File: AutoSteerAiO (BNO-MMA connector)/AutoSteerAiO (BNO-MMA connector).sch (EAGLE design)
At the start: 83 parts, among them J4 CONNECTOR 1x5 PINS, K4 CB1A-P-12V, U1 VX7805-1000

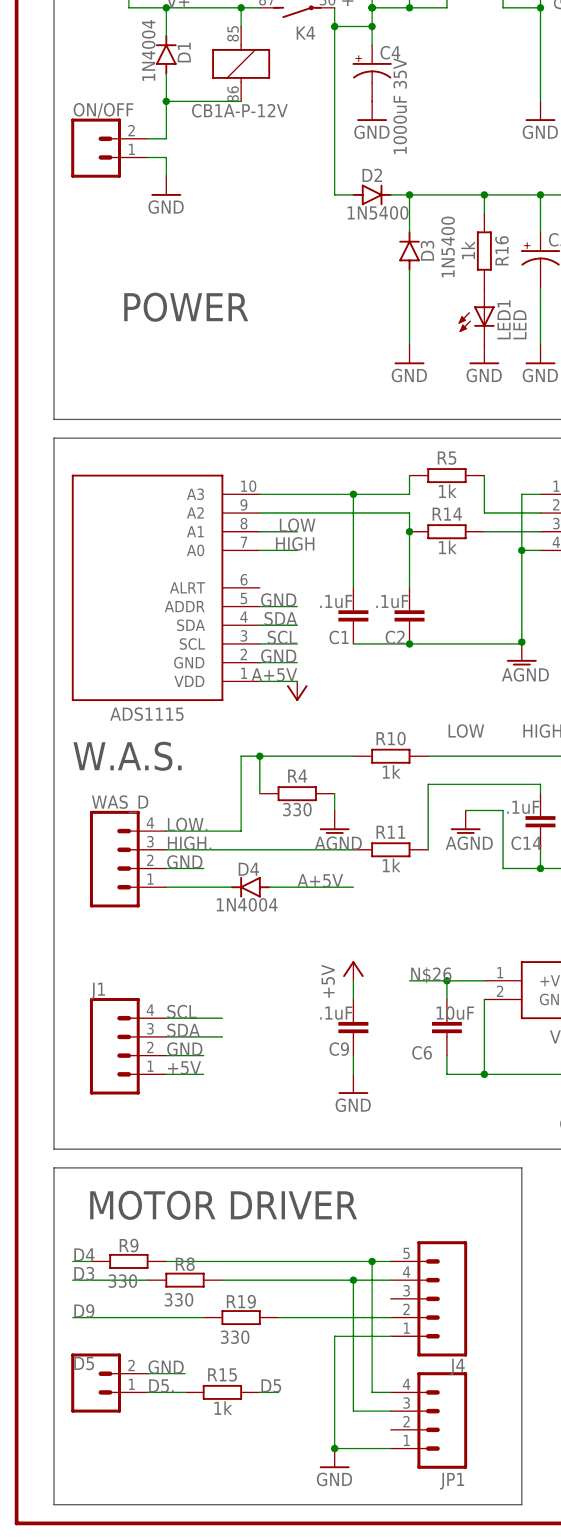
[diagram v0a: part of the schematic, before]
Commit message: Add files via upload
added led autosteer
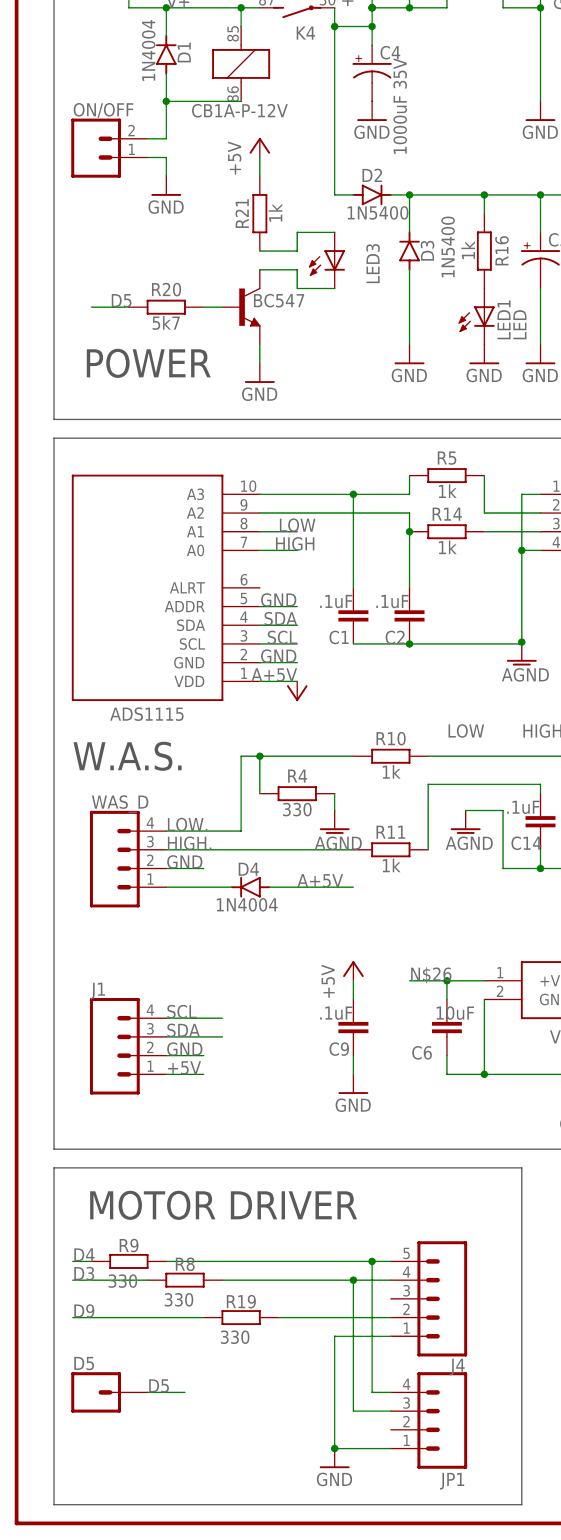
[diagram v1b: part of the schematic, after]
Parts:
- removed R15: 1k, resistor:R-EU_0207/7
- added LED3: LED, adafruit:LED5MM
- added R20: 5k7, resistor:R-EU_0207/7
- added R21: 1k, resistor:R-EU_0207/7
- added T1: BC547, transistor:BC547
- D5: device SparkFun-Connectors:CONN_02 -> SparkFun-Connectors:CONN_01
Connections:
- removed net D5.: D5.1, R15.1
- new net N$23: R20.2, T1.B
- new net N$24: LED3.A, R21.1
- new net N$27: LED3.C, T1.C
- net +5V: now also R21.2
- net D5: now also D5.1, R20.1; no longer R15.2
- net GND: now also T1.E; no longer D5.2
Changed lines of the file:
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@@
 <attribute name="OC_NEWARK" value="unknown"/>
 </part>
-<part name="D5" library="SparkFun-Connectors" library_urn="urn:adsk.eagle:library:513" deviceset="CONN_02" device="" package3d_urn="urn:adsk.eagle:package:38039/1" value="CONNECTOR 1x1 PIN">
+<part name="D5" library="SparkFun-Connectors" library_urn="urn:adsk.eagle:library:513" deviceset="CONN_01" device="" package3d_urn="urn:adsk.eagle:package:38028/1" value="CONNECTOR 1x1 PIN">
 <attribute name="MF" value=""/>
 <attribute name="MPN" value=""/>
@@
 <attribute name="OC_NEWARK" value="unknown"/>
 </part>
-<part name="R15" library="resistor" library_urn="urn:adsk.eagle:library:348" deviceset="R-EU_" device="0207/7" package3d_urn="urn:adsk.eagle:package:23493/2" value="1k">
-<attribute name="MF" value=""/>
-<attribute name="MPN" value=""/>
-<attribute name="OC_NEWARK" value="unknown"/>
-</part>
 <part name="J1" library="SparkFun-Connectors" library_urn="urn:adsk.eagle:library:513" deviceset="CONN_04" device="" package3d_urn="urn:adsk.eagle:package:38085/1"/>
 <part name="J2" library="SparkFun-Connectors" library_urn="urn:adsk.eagle:library:513" deviceset="CONN_05" device="" package3d_urn="urn:adsk.eagle:package:38104/1"/>
@@
 <part name="GND11" library="supply1" library_urn="urn:adsk.eagle:library:371" deviceset="GND" device=""/>
 <part name="P+3" library="supply1" library_urn="urn:adsk.eagle:library:371" deviceset="+5V" device=""/>
+<part name="T1" library="transistor" library_urn="urn:adsk.eagle:library:402" deviceset="BC547" device="" package3d_urn="urn:adsk.eagle:package:28523/2"/>
+<part name="R20" library="resistor" library_urn="urn:adsk.eagle:library:348" deviceset="R-EU_" device="0207/7" package3d_urn="urn:adsk.eagle:package:23493/2" value="5k7">
+<attribute name="MF" value=""/>
+<attribute name="MPN" value=""/>
+<attribute name="OC_NEWARK" value="unknown"/>
+</part>
+<part name="R21" library="resistor" library_urn="urn:adsk.eagle:library:348" deviceset="R-EU_" device="0207/7" package3d_urn="urn:adsk.eagle:package:23493/2" value="1k">
+<attribute name="MF" value=""/>
+<attribute name="MPN" value=""/>
+<attribute name="OC_NEWARK" value="unknown"/>
+</part>
+<part name="P+6" library="supply1" library_urn="urn:adsk.eagle:library:371" deviceset="+5V" device=""/>
+<part name="GND12" library="supply1" library_urn="urn:adsk.eagle:library:371" deviceset="GND" device=""/>
+<part name="LED3" library="adafruit" library_urn="urn:adsk.eagle:library:420" deviceset="LED" device="5MM" package3d_urn="urn:adsk.eagle:package:6240538/1" value="LED">
+<attribute name="MF" value=""/>
+<attribute name="MPN" value=""/>
+<attribute name="OC_NEWARK" value="unknown"/>
+</part>
 </parts>
 <sheets>
@@
 <wire x1="144.78" y1="213.36" x2="144.78" y2="284.48" width="0.1524" layer="97"/>
 <wire x1="144.78" y1="213.36" x2="5.08" y2="213.36" width="0.1524" layer="97"/>
-<text x="22.86" y="228.6" size="3.81" layer="97" font="vector" align="center">POWER</text>
+<text x="17.78" y="220.98" size="3.81" layer="97" font="vector" align="center">POWER</text>
 <wire x1="147.32" y1="198.12" x2="147.32" y2="256.54" width="0.1524" layer="97"/>
 <wire x1="205.74" y1="198.12" x2="147.32" y2="198.12" width="0.1524" layer="97"/>
@@
 <attribute name="MPN" x="152.4" y="276.86" size="1.778" layer="96" display="off"/>
 </instance>
-<instance part="R15" gate="G$1" x="27.94" y="81.28" smashed="yes">
-<attribute name="NAME" x="27.94" y="82.7786" size="1.778" layer="95" rot="R180" align="top-center"/>
-<attribute name="VALUE" x="27.94" y="80.01" size="1.778" layer="95" rot="R180" align="bottom-center"/>
-<attribute name="OC_NEWARK" x="27.94" y="81.28" size="1.778" layer="96" display="off"/>
-<attribute name="MF" x="27.94" y="81.28" size="1.778" layer="96" display="off"/>
-<attribute name="MPN" x="27.94" y="81.28" size="1.778" layer="96" display="off"/>
-</instance>
 <instance part="J1" gate="G$1" x="15.24" y="127" smashed="yes">
 <attribute name="VALUE" x="10.16" y="119.634" size="1.778" layer="96" font="vector"/>
@@
 <instance part="P+3" gate="1" x="111.76" y="190.5" smashed="yes">
 <attribute name="VALUE" x="109.22" y="185.42" size="1.778" layer="96" rot="R90"/>
+</instance>
+<instance part="T1" gate="G$1" x="30.48" y="228.6" smashed="yes">
+<attribute name="VALUE" x="32.004" y="228.6" size="1.778" layer="96"/>
+</instance>
+<instance part="R20" gate="G$1" x="20.32" y="228.6" smashed="yes">
+<attribute name="NAME" x="20.32" y="230.0986" size="1.778" layer="95" rot="R180" align="top-center"/>
+<attribute name="VALUE" x="20.32" y="227.33" size="1.778" layer="95" rot="R180" align="bottom-center"/>
+<attribute name="OC_NEWARK" x="20.32" y="228.6" size="1.778" layer="96" display="off"/>
+<attribute name="MF" x="20.32" y="228.6" size="1.778" layer="96" display="off"/>
+<attribute name="MPN" x="20.32" y="228.6" size="1.778" layer="96" display="off"/>
+</instance>
+<instance part="R21" gate="G$1" x="33.02" y="241.3" smashed="yes" rot="R90">
+<attribute name="NAME" x="31.5214" y="241.3" size="1.778" layer="95" rot="R270" align="top-center"/>
+<attribute name="VALUE" x="34.29" y="241.3" size="1.778" layer="95" rot="R270" align="bottom-center"/>
+<attribute name="OC_NEWARK" x="33.02" y="241.3" size="1.778" layer="96" rot="R90" display="off"/>
+<attribute name="MF" x="33.02" y="241.3" size="1.778" layer="96" rot="R90" display="off"/>
+<attribute name="MPN" x="33.02" y="241.3" size="1.778" layer="96" rot="R90" display="off"/>
+</instance>
+<instance part="P+6" gate="1" x="33.02" y="251.46" smashed="yes">
+<attribute name="VALUE" x="30.48" y="246.38" size="1.778" layer="96" rot="R90"/>
+</instance>
+<instance part="GND12" gate="1" x="33.02" y="218.44" smashed="yes">
+<attribute name="VALUE" x="30.48" y="215.9" size="1.778" layer="96"/>
+</instance>
+<instance part="LED3" gate="G$1" x="43.18" y="236.22" smashed="yes">
+<attribute name="NAME" x="49.276" y="231.648" size="1.778" layer="95" rot="R90"/>
+<attribute name="OC_NEWARK" x="43.18" y="236.22" size="1.778" layer="96" display="off"/>
+<attribute name="MF" x="43.18" y="236.22" size="1.778" layer="96" display="off"/>
+<attribute name="MPN" x="43.18" y="236.22" size="1.778" layer="96" display="off"/>
 </instance>
 </instances>
@@
 <wire x1="96.52" y1="154.94" x2="101.6" y2="154.94" width="0.1524" layer="91"/>
 <label x="96.52" y="154.94" size="1.778" layer="95"/>
+</segment>
+<segment>
+<pinref part="R21" gate="G$1" pin="2"/>
+<pinref part="P+6" gate="1" pin="+5V"/>
+<wire x1="33.02" y1="248.92" x2="33.02" y2="246.38" width="0.1524" layer="91"/>
 </segment>
 </net>
@@
 </segment>
 <segment>
-<pinref part="D5" gate="G$1" pin="2"/>
-<wire x1="17.78" y1="83.82" x2="22.86" y2="83.82" width="0.1524" layer="91"/>
-<label x="17.78" y="83.82" size="1.778" layer="95"/>
-</segment>
-<segment>
 <pinref part="0" gate="J$1" pin="3"/>
 <wire x1="177.8" y1="279.4" x2="180.34" y2="279.4" width="0.1524" layer="91"/>
@@
 <pinref part="GND11" gate="1" pin="GND"/>
 </segment>
+<segment>
+<pinref part="T1" gate="G$1" pin="E"/>
+<pinref part="GND12" gate="1" pin="GND"/>
+<wire x1="33.02" y1="220.98" x2="33.02" y2="223.52" width="0.1524" layer="91"/>
+</segment>
 </net>
 <net name="D5" class="0">
@@
 </segment>
 <segment>
-<pinref part="R15" gate="G$1" pin="2"/>
-<wire x1="33.02" y1="81.28" x2="35.56" y2="81.28" width="0.1524" layer="91"/>
-<label x="33.02" y="81.28" size="1.778" layer="95"/>
+<wire x1="15.24" y1="228.6" x2="10.16" y2="228.6" width="0.1524" layer="91"/>
+<pinref part="R20" gate="G$1" pin="1"/>
+<label x="12.7" y="228.6" size="1.778" layer="95"/>
+</segment>
+<segment>
+<pinref part="D5" gate="G$1" pin="1"/>
+<wire x1="17.78" y1="81.28" x2="22.86" y2="81.28" width="0.1524" layer="91"/>
+<label x="17.78" y="81.28" size="1.778" layer="95"/>
 </segment>
 </net>
@@
 </segment>
 </net>
-<net name="D5." class="0">
-<segment>
-<pinref part="D5" gate="G$1" pin="1"/>
-<wire x1="17.78" y1="81.28" x2="22.86" y2="81.28" width="0.1524" layer="91"/>
-<label x="17.78" y="81.28" size="1.778" layer="95"/>
-<pinref part="R15" gate="G$1" pin="1"/>
-</segment>
-</net>
+<net name="N$23" class="0">
+<segment>
+<wire x1="25.4" y1="228.6" x2="27.94" y2="228.6" width="0.1524" layer="91"/>
+<pinref part="T1" gate="G$1" pin="B"/>
+<pinref part="R20" gate="G$1" pin="2"/>
+</segment>
+</net>
+<net name="N$24" class="0">
+<segment>
+<wire x1="43.18" y1="238.76" x2="38.1" y2="238.76" width="0.1524" layer="91"/>
+<wire x1="38.1" y1="238.76" x2="38.1" y2="236.22" width="0.1524" layer="91"/>
+<pinref part="R21" gate="G$1" pin="1"/>
+<wire x1="38.1" y1="236.22" x2="33.02" y2="236.22" width="0.1524" layer="91"/>
+<pinref part="LED3" gate="G$1" pin="A"/>
+</segment>
+</net>
+<net name="N$27" class="0">
+<segment>
+<pinref part="T1" gate="G$1" pin="C"/>
+<wire x1="33.02" y1="233.68" x2="38.1" y2="233.68" width="0.1524" layer="91"/>
+<wire x1="38.1" y1="233.68" x2="38.1" y2="231.14" width="0.1524" layer="91"/>
+<wire x1="38.1" y1="231.14" x2="43.18" y2="231.14" width="0.1524" layer="91"/>
+<pinref part="LED3" gate="G$1" pin="C"/>
+</segment>
+</net>

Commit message: Add files via upload
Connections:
- net N$25: now also R16.1
- net N$26: no longer R16.1
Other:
- moved on the sheet: LED1, R16
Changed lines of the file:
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@@
 </instance>
 <instance part="P+4" gate="1" x="38.1" y="175.26" smashed="yes" rot="R180"/>
-<instance part="LED1" gate="G$1" x="63.5" y="228.6" smashed="yes">
-<attribute name="NAME" x="67.056" y="224.028" size="1.778" layer="95" rot="R90"/>
-<attribute name="VALUE" x="69.215" y="224.028" size="1.778" layer="96" rot="R90"/>
-<attribute name="OC_NEWARK" x="63.5" y="228.6" size="1.778" layer="96" display="off"/>
-<attribute name="MF" x="63.5" y="228.6" size="1.778" layer="96" display="off"/>
-<attribute name="MPN" x="63.5" y="228.6" size="1.778" layer="96" display="off"/>
-</instance>
-<instance part="R16" gate="G$1" x="63.5" y="236.22" smashed="yes" rot="R270">
-<attribute name="NAME" x="64.9986" y="236.22" size="1.778" layer="95" rot="R90" align="top-center"/>
-<attribute name="VALUE" x="62.23" y="236.22" size="1.778" layer="95" rot="R90" align="bottom-center"/>
-<attribute name="OC_NEWARK" x="63.5" y="236.22" size="1.778" layer="96" display="off"/>
-<attribute name="MF" x="63.5" y="236.22" size="1.778" layer="96" display="off"/>
-<attribute name="MPN" x="63.5" y="236.22" size="1.778" layer="96" display="off"/>
-</instance>
-<instance part="GND14" gate="1" x="63.5" y="220.98" smashed="yes">
-<attribute name="VALUE" x="60.96" y="218.44" size="1.778" layer="96"/>
+<instance part="LED1" gate="G$1" x="121.92" y="129.54" smashed="yes">
+<attribute name="NAME" x="125.476" y="124.968" size="1.778" layer="95" rot="R90"/>
+<attribute name="VALUE" x="127.635" y="124.968" size="1.778" layer="96" rot="R90"/>
+<attribute name="OC_NEWARK" x="121.92" y="129.54" size="1.778" layer="96" display="off"/>
+<attribute name="MF" x="121.92" y="129.54" size="1.778" layer="96" display="off"/>
+<attribute name="MPN" x="121.92" y="129.54" size="1.778" layer="96" display="off"/>
+</instance>
+<instance part="R16" gate="G$1" x="121.92" y="137.16" smashed="yes" rot="R270">
+<attribute name="NAME" x="123.4186" y="137.16" size="1.778" layer="95" rot="R90" align="top-center"/>
+<attribute name="VALUE" x="120.65" y="137.16" size="1.778" layer="95" rot="R90" align="bottom-center"/>
+<attribute name="OC_NEWARK" x="121.92" y="137.16" size="1.778" layer="96" display="off"/>
+<attribute name="MF" x="121.92" y="137.16" size="1.778" layer="96" display="off"/>
+<attribute name="MPN" x="121.92" y="137.16" size="1.778" layer="96" display="off"/>
+</instance>
+<instance part="GND14" gate="1" x="121.92" y="121.92" smashed="yes">
+<attribute name="VALUE" x="119.38" y="119.38" size="1.778" layer="96"/>
 </instance>
 <instance part="GND23" gate="1" x="83.82" y="220.98" smashed="yes">
@@
 <wire x1="50.8" y1="243.84" x2="53.34" y2="243.84" width="0.1524" layer="91"/>
 <pinref part="C5" gate="G$1" pin="+"/>
-<wire x1="53.34" y1="243.84" x2="63.5" y2="243.84" width="0.1524" layer="91"/>
-<wire x1="63.5" y1="243.84" x2="71.12" y2="243.84" width="0.1524" layer="91"/>
+<wire x1="53.34" y1="243.84" x2="71.12" y2="243.84" width="0.1524" layer="91"/>
 <wire x1="71.12" y1="243.84" x2="83.82" y2="243.84" width="0.1524" layer="91"/>
 <wire x1="71.12" y1="238.76" x2="71.12" y2="243.84" width="0.1524" layer="91"/>
 <junction x="71.12" y="243.84"/>
-<pinref part="R16" gate="G$1" pin="1"/>
-<wire x1="63.5" y1="241.3" x2="63.5" y2="243.84" width="0.1524" layer="91"/>
-<junction x="63.5" y="243.84"/>
 <pinref part="U1" gate="G$1" pin="+VIN"/>
 <junction x="83.82" y="243.84"/>
@@
 <wire x1="96.52" y1="134.62" x2="96.52" y2="137.16" width="0.1524" layer="91"/>
 <junction x="96.52" y="137.16"/>
-</segment>
-</net>
+<wire x1="96.52" y1="137.16" x2="96.52" y2="142.24" width="0.1524" layer="91"/>
+<pinref part="R16" gate="G$1" pin="1"/>
+<wire x1="96.52" y1="142.24" x2="121.92" y2="142.24" width="0.1524" layer="91"/>
+</segment>
+</net>

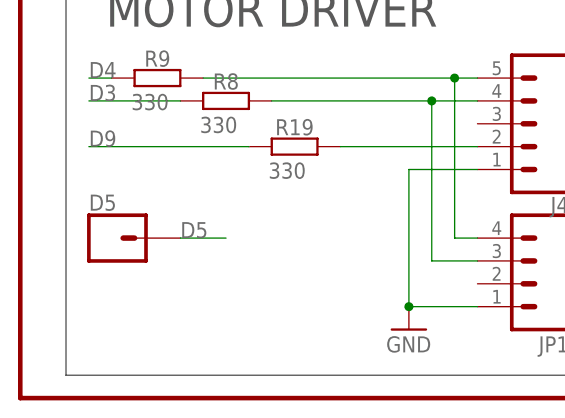
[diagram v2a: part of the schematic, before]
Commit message: Add files via upload
Adeed 5V connector for IBT2
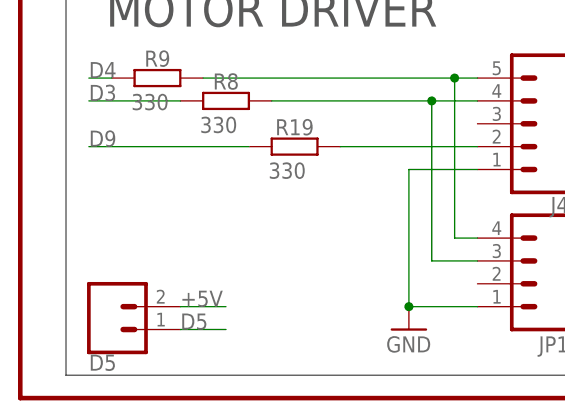
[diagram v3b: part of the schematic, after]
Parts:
- D5: device SparkFun-Connectors:CONN_01 -> SparkFun-Connectors:CONN_02
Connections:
- net +5V: now also D5.2
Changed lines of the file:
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@@
-<attribute name="OC_NEWARK" value="unknown"/>
-</part>
-<part name="D5" library="SparkFun-Connectors" library_urn="urn:adsk.eagle:library:513" deviceset="CONN_01" device="" package3d_urn="urn:adsk.eagle:package:38028/1" value="CONNECTOR 1x1 PIN">
-<attribute name="MF" value=""/>
-<attribute name="MPN" value=""/>
 <attribute name="OC_NEWARK" value="unknown"/>
 </part>
@@
 <attribute name="OC_NEWARK" value="unknown"/>
 </part>
+<part name="D5" library="SparkFun-Connectors" library_urn="urn:adsk.eagle:library:513" deviceset="CONN_02" device="" package3d_urn="urn:adsk.eagle:package:38039/1" value="CONNECTOR 1x1 PIN">
+<attribute name="MF" value=""/>
+<attribute name="MPN" value=""/>
+<attribute name="OC_NEWARK" value="unknown"/>
+</part>
 </parts>
 <sheets>
@@
 <attribute name="MPN" x="127" y="233.68" size="1.778" layer="96" display="off"/>
 </instance>
-<instance part="D5" gate="G$1" x="10.16" y="81.28" smashed="yes">
-<attribute name="NAME" x="7.62" y="84.328" size="1.778" layer="95" font="vector"/>
-<attribute name="OC_NEWARK" x="10.16" y="81.28" size="1.778" layer="96" rot="R90" display="off"/>
-<attribute name="MF" x="10.16" y="81.28" size="1.778" layer="96" rot="R90" display="off"/>
-<attribute name="MPN" x="10.16" y="81.28" size="1.778" layer="96" rot="R90" display="off"/>
-</instance>
 <instance part="0" gate="J$1" x="170.18" y="276.86" smashed="yes">
 <attribute name="NAME" x="167.64" y="282.448" size="1.778" layer="95" font="vector"/>
@@
 <attribute name="MF" x="43.18" y="236.22" size="1.778" layer="96" display="off"/>
 <attribute name="MPN" x="43.18" y="236.22" size="1.778" layer="96" display="off"/>
+</instance>
+<instance part="D5" gate="G$1" x="10.16" y="71.12" smashed="yes">
+<attribute name="NAME" x="7.62" y="66.548" size="1.778" layer="95" font="vector"/>
+<attribute name="OC_NEWARK" x="10.16" y="71.12" size="1.778" layer="96" rot="R90" display="off"/>
+<attribute name="MF" x="10.16" y="71.12" size="1.778" layer="96" rot="R90" display="off"/>
+<attribute name="MPN" x="10.16" y="71.12" size="1.778" layer="96" rot="R90" display="off"/>
 </instance>
 </instances>
@@
 <pinref part="P+6" gate="1" pin="+5V"/>
 <wire x1="33.02" y1="248.92" x2="33.02" y2="246.38" width="0.1524" layer="91"/>
+</segment>
+<segment>
+<pinref part="D5" gate="G$1" pin="2"/>
+<wire x1="17.78" y1="73.66" x2="22.86" y2="73.66" width="0.1524" layer="91"/>
+<label x="17.78" y="73.66" size="1.778" layer="95"/>
 </segment>
 </net>
@@
 <segment>
 <pinref part="D5" gate="G$1" pin="1"/>
-<wire x1="17.78" y1="81.28" x2="22.86" y2="81.28" width="0.1524" layer="91"/>
-<label x="17.78" y="81.28" size="1.778" layer="95"/>
+<wire x1="17.78" y1="71.12" x2="22.86" y2="71.12" width="0.1524" layer="91"/>
+<label x="17.78" y="71.12" size="1.778" layer="95"/>
 </segment>
 </net>
